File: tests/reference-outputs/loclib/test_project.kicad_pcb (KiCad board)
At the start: 8 copper layers, 57.6 x 50 mm, 73 parts, among them J1 HDMI_A, J2 Conn_01x02_Pin, J3 Barrel_Jack_MountingPin, J4 Conn_01x35_Pin, U1 ASDMB-xxxMHz, U2 ADV7611, U3 LM3880, U4 AP2112K-1.8, U6 RT9742AGJ5F

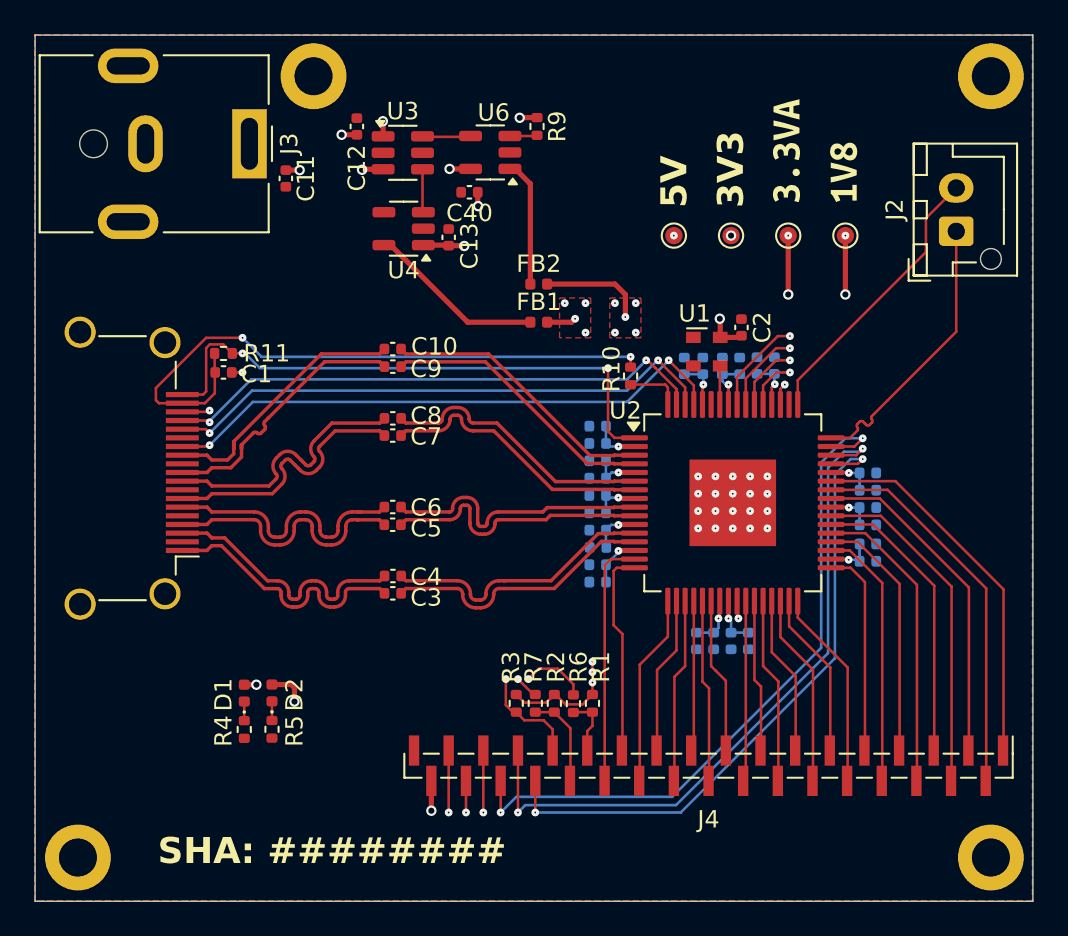
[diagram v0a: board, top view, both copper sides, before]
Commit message: [#68432] Add design errors to PCB
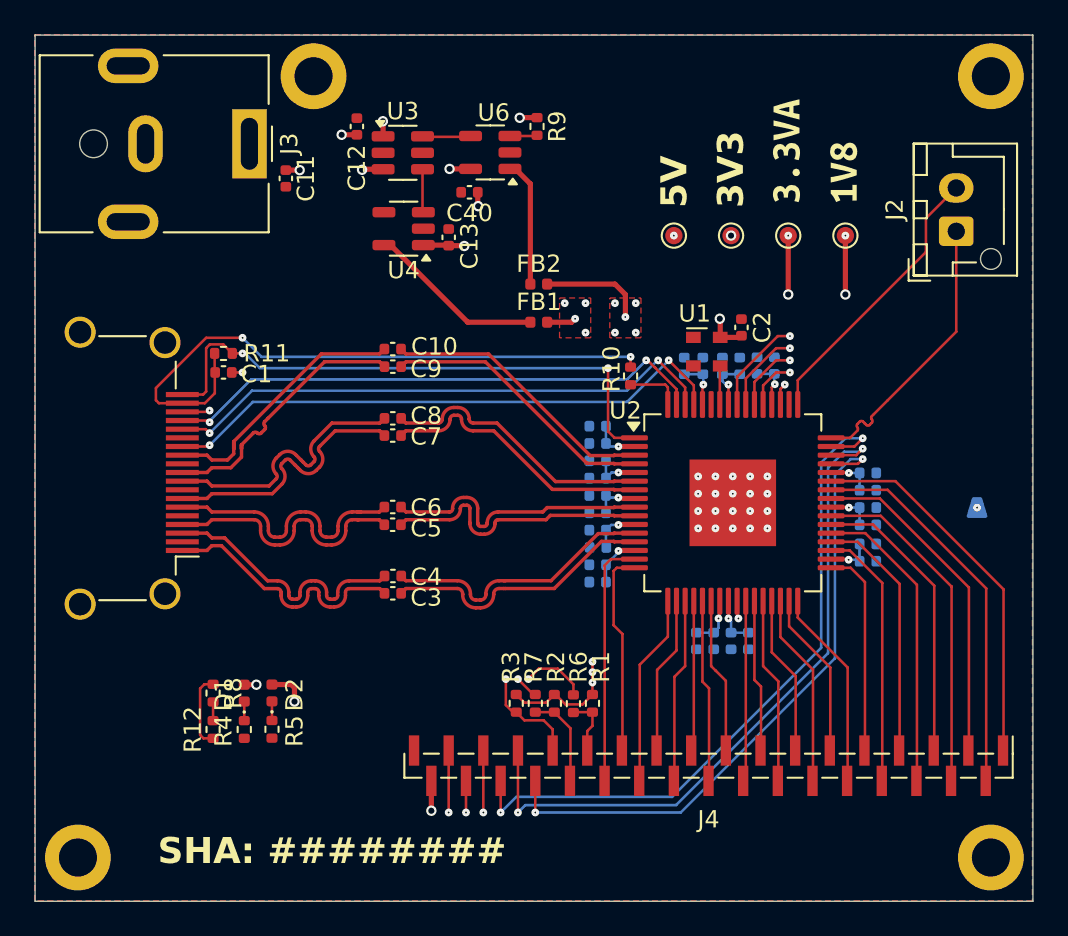
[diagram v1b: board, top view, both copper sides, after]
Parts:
- added R12: 220, test_project-footprints:R_0402_1005Metric, F.Cu at (130.2, 158.6)
- added R8: 220, test_project-footprints:R_0402_1005Metric, F.Cu at (130.2, 156.5)
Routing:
- net (no net): track 0.00 -> 5.44 mm
- net +1V8: vias 15 -> 16
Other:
- board text added: "Polygon with net assigned"

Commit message: [#70870] Update test design rebase
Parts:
- removed H4: MountingHole_Pad, test_project-footprints:MountingHole_2.2mm_M2_DIN965_Pad
- removed kibuzzard-671B6B39: G***, kibuzzard-671B6B39
- removed kibuzzard-671B7834: G***, kibuzzard-671B7834
- added D3: PESD3V3L4UG, test_project-footprints:SOT-353_SC-70-5, F.Cu at (132.0, 132.7)
- added REF**: C_0402_1005Metric, test_project-footprints:C_0402_1005Metric, F.Cu at (147.4, 119.9)
- added REF**: C_0402_1005Metric, test_project-footprints:C_0402_1005Metric, F.Cu at (154.6, 120.8)
- added REF**: C_0402_1005Metric, test_project-footprints:C_0402_1005Metric, F.Cu at (167.5, 120.7)
- added REF**: C_0402_1005Metric, test_project-footprints:C_0402_1005Metric, F.Cu at (148.4, 119.9)
- added kibuzzard-67891633: G***, kibuzzard-67891633, F.Cu at (163.4, 126.0)
- added kibuzzard-67891646: G***, kibuzzard-67891646, F.Cu at (166.6, 126.6)
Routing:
- net /Connectors/hdmi_in.CEC: track 33.3 -> 50.7 mm
- net /Connectors/hdmi_in.SDA: track 31.7 -> 47.1 mm
- net /Connectors/hdmi_in.SCL: track 32.5 -> 47.6 mm
- net /Connectors/hdmi_in.HPD: track 33.1 -> 40.2 mm
- net +3.3VA: track 46.1 -> 52.1 mm
- net GND: track 2.23 -> 3.27 mm, vias 22 -> 26
- added copper zone on B.Cu, net +3.3VA
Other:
- outline, holes or cut-outs redrawn
- board text added: "Edge.Cuts hole"
- board text added: "Footprint overrides Custom polygon pad"
- board text added: "Micro Burried Blind Removed annular ring"
- board text added: "Not in schematic Non standard rotation angle"
- board text added: "Text with non-default font"
- board text added: "Variable company name: ${COMPANY}"
- board text added: "Zone connected only on F.Cu and B.Cu"

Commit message: [#75441] Kicad9
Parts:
- added R13: 100k, test_project-footprints:R_0402_1005Metric, B.Cu at (138.5, 129.4)
- added R14: 100k, test_project-footprints:R_0402_1005Metric, B.Cu at (138.5, 131.9)
- added R15: 100k, test_project-footprints:R_0402_1005Metric, B.Cu at (137.0, 130.6)
- added R16: 100k, test_project-footprints:R_0402_1005Metric, B.Cu at (140.0, 130.6)
- added R17: 100k, test_project-footprints:R_0402_1005Metric, B.Cu at (132.5, 130.7)
- added R18: 100k, test_project-footprints:R_0402_1005Metric, B.Cu at (131.0, 129.5)
- added R19: 100k, test_project-footprints:R_0402_1005Metric, B.Cu at (131.0, 132.0)
- added R20: 100k, test_project-footprints:R_0402_1005Metric, B.Cu at (129.5, 130.7)
- added TP5: TestPoint, test_project-footprints:TestPoint_Pad_D1.0mm, B.Cu at (136.8, 132.2)
- added TP6: TestPoint, test_project-footprints:TestPoint_Pad_D1.0mm, B.Cu at (140.1, 129.0)
- added TP7: TestPoint, test_project-footprints:TestPoint_Pad_D1.0mm, B.Cu at (132.6, 129.1)
- added TP8: TestPoint, test_project-footprints:TestPoint_Pad_D1.0mm, B.Cu at (129.3, 132.3)
- D3: moved to B.Cu
- moved D3 7.84 mm to (132.0, 140.5), turned to 90 degrees
- moved C1 1.46 mm to (129.4, 137.6), turned to 90 degrees
- moved R11 0.76 mm to (130.5, 137.6), turned to -90 degrees
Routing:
- net /Connectors/hdmi_in.CEC: track 50.7 -> 34.1 mm
- net /Connectors/hdmi_in.SCL: track 47.6 -> 32.9 mm
- net /Connectors/hdmi_in.SDA: track 47.1 -> 32.6 mm
- net /Connectors/hdmi_in.HPD: track 40.2 -> 32.9 mm
- net GND: track 3.27 -> 9.19 mm
- net +5V: track 44.3 -> 39.0 mm
- net Net-(R17-Pad1): track 0.00 -> 3.45 mm
- net Net-(R13-Pad1): track 0.00 -> 3.45 mm
- net Net-(R17-Pad2): track 0.00 -> 1.77 mm
- net Net-(R16-Pad2): track 0.00 -> 1.77 mm
- net +3V3: track 71.7 -> 73.4 mm, vias 10 -> 11
- net Net-(R15-Pad1): track 0.00 -> 1.73 mm
- net Net-(R20-Pad1): track 0.00 -> 1.73 mm
- net (no net): vias 0 -> 3
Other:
- outline, holes or cut-outs redrawn
- board text added: "${DRC_ERROR Check SI} Manual DRC ERROR"
- board text added: "${DRC_WARNING Clean texts} Manual DRC WARNING"
- board text added: "<- Via with changed tenting"
- board text added: "<- Via with padstack 1"
- board text added: "<- Via with padstack 2"
- board text added: "Changed PTH padstack ->"
